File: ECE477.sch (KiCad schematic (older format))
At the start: 54 parts, among them IC1 LP3852EMP-3.3_NOPB, IC5 BQ29330DBT, J1 P7805-2000-S, U1 STM32H7_LQFP144_T2

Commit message: Added Pinout
Added footprints and pinout connections
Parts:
- removed J? (x3): Conn_01x05_Male, symbol Connector:Conn_01x05_Male
- IC5: footprint SOP50P640X120-30N -> SamacSys_Parts:SOP50P640X120-30N
- J2: renamed from J?; footprint (none) -> Connector_PinHeader_1.00mm:PinHeader_1x06_P1.00mm_Vertical
- J3, J4: renamed from J?; footprint (none) -> Connector_PinHeader_1.00mm:PinHeader_1x05_P1.00mm_Vertical
- SW1: renamed from SW?; footprint (none) -> Button_Switch_THT:SW_TH_Tactile_Omron_B3F-10xx
- gave numbers to parts that had none: 3
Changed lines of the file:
@@
 F 0 "IC5" H 9062 1786 50  0000 C CNN
 F 1 "BQ29330DBT" H 9055 1673 50  0000 C CNN
-F 2 "SOP50P640X120-30N" H 19650 4000 50  0001 L CNN
+F 2 "SamacSys_Parts:SOP50P640X120-30N" H 19650 4000 50  0001 L CNN
 F 3 "http://www.ti.com/general/docs/suppproductinfo.tsp?distId=26&gotoUrl=http%3A%2F%2Fwww.ti.com%2Flit%2Fgpn%2Fbq29330" H 19650 3900 50  0001 L CNN
 F 4 "TEXAS INSTRUMENTS - BQ29330DBT. - Li-Ion Battery, Li-Pol Full Protector, 2/3/4 Series, I2C interface, 4.5 V to 28 V supply, TSSOP-30" H 19650 3800 50  0001 L CNN "Description"
@@
 LEDs \nPWR swtch\nmake sure GPIO are ocnnected to advanced timers\n\n\n\n
 $Comp
-L Switch:SW_Push_Dual SW?
+L Switch:SW_Push_Dual SW1
 U 1 1 5F877F07
 P 5850 13350
-F 0 "SW?" H 5850 13635 50  0000 C CNN
+F 0 "SW1" H 5850 13635 50  0000 C CNN
 F 1 "SW_Push_Dual" H 5850 13544 50  0000 C CNN
-F 2 "" H 5850 13550 50  0001 C CNN
+F 2 "Button_Switch_THT:SW_TH_Tactile_Omron_B3F-10xx" H 5850 13550 50  0001 C CNN
 F 3 "~" H 5850 13550 50  0001 C CNN
 	1    5850 13350
@@
 $EndComp
 $Comp
-L pspice:CAP C?
+L pspice:CAP C30
 U 1 1 5F887729
 P 6600 13450
-F 0 "C?" H 6778 13496 50  0000 L CNN
+F 0 "C30" H 6778 13496 50  0000 L CNN
 F 1 ".1uF" H 6778 13405 50  0000 L CNN
 F 2 "Capacitor_SMD:C_0805_2012Metric_Pad1.15x1.40mm_HandSolder" H 6600 13450 50  0001 C CNN
@@
 $EndComp
 $Comp
-L Device:R_US R?
+L Device:R_US R3
 U 1 1 5F8954D3
 P 5850 12600
-F 0 "R?" H 5918 12646 50  0000 L CNN
+F 0 "R3" H 5918 12646 50  0000 L CNN
 F 1 "100k" H 5918 12555 50  0000 L CNN
 F 2 "Resistor_SMD:R_0805_2012Metric_Pad1.15x1.40mm_HandSolder" V 5890 12590 50  0001 C CNN
@@
 VDD_MCU
 $Comp
-L power:GND #PWR?
+L power:GND #PWR05
 U 1 1 5F9369F7
 P 5850 13900
-F 0 "#PWR?" H 5850 13650 50  0001 C CNN
+F 0 "#PWR05" H 5850 13650 50  0001 C CNN
 F 1 "GND" H 5855 13727 50  0000 C CNN
 F 2 "" H 5850 13900 50  0001 C CNN
@@
 NRST
 $Comp
-L Device:R_US R?
+L Device:R_US R4
 U 1 1 5F993DC3
 P 22300 3750
-F 0 "R?" H 22368 3796 50  0000 L CNN
+F 0 "R4" H 22368 3796 50  0000 L CNN
 F 1 "100k" H 22368 3705 50  0000 L CNN
 F 2 "Resistor_SMD:R_0805_2012Metric_Pad1.15x1.40mm_HandSolder" V 22340 3740 50  0001 C CNN
@@
 BOOT0
 $Comp
-L power:GND #PWR?
+L power:GND #PWR06
 U 1 1 5F9EC431
 P 22650 3750
-F 0 "#PWR?" H 22650 3500 50  0001 C CNN
+F 0 "#PWR06" H 22650 3500 50  0001 C CNN
 F 1 "GND" H 22655 3577 50  0000 C CNN
 F 2 "" H 22650 3750 50  0001 C CNN
@@
 $EndComp
 $Comp
-L Connector:Conn_01x06_Male J?
+L Connector:Conn_01x06_Male J2
 U 1 1 5FA28754
 P 10600 8950
-F 0 "J?" H 10708 9331 50  0000 C CNN
+F 0 "J2" H 10708 9331 50  0000 C CNN
 F 1 "Conn_01x05_Male" H 10708 9240 50  0000 C CNN
-F 2 "" H 10600 8950 50  0001 C CNN
+F 2 "Connector_PinHeader_1.00mm:PinHeader_1x06_P1.00mm_Vertical" H 10600 8950 50  0001 C CNN
 F 3 "~" H 10600 8950 50  0001 C CNN
 	1    10600 8950
@@
 $EndComp
 $Comp
-L Connector:Conn_01x05_Male J?
+L Connector:Conn_01x05_Male J4
 U 1 1 5FA2B098
 P 12150 9000
-F 0 "J?" H 12258 9381 50  0000 C CNN
+F 0 "J4" H 12258 9381 50  0000 C CNN
 F 1 "Conn_01x05_Male" H 12258 9290 50  0000 C CNN
-F 2 "" H 12150 9000 50  0001 C CNN
+F 2 "Connector_PinHeader_1.00mm:PinHeader_1x05_P1.00mm_Vertical" H 12150 9000 50  0001 C CNN
 F 3 "~" H 12150 9000 50  0001 C CNN
 	1    12150 9000
@@
 $EndComp
 $Comp
-L Connector:Conn_01x05_Male J?
+L Connector:Conn_01x05_Male J3
 U 1 1 5FA398AC
 P 11800 7550
-F 0 "J?" H 11908 7931 50  0000 C CNN
+F 0 "J3" H 11908 7931 50  0000 C CNN
 F 1 "Conn_01x05_Male" H 11908 7840 50  0000 C CNN
-F 2 "" H 11800 7550 50  0001 C CNN
+F 2 "Connector_PinHeader_1.00mm:PinHeader_1x05_P1.00mm_Vertical" H 11800 7550 50  0001 C CNN
 F 3 "~" H 11800 7550 50  0001 C CNN
 	1    11800 7550
 	1    0    0    -1
 $EndComp
-$Comp
-L Connector:Conn_01x05_Male J?
-U 1 1 5FA48124
-P 15350 10200
-F 0 "J?" H 15458 10581 50  0000 C CNN
-F 1 "Conn_01x05_Male" H 15458 10490 50  0000 C CNN
-F 2 "" H 15350 10200 50  0001 C CNN
-F 3 "~" H 15350 10200 50  0001 C CNN
-	1    15350 10200
-	1    0    0    -1
-$EndComp
-$Comp
-L Connector:Conn_01x05_Male J?
-U 1 1 5FA567D5
-P 16050 10200
-F 0 "J?" H 16158 10581 50  0000 C CNN
-F 1 "Conn_01x05_Male" H 16158 10490 50  0000 C CNN
-F 2 "" H 16050 10200 50  0001 C CNN
-F 3 "~" H 16050 10200 50  0001 C CNN
-	1    16050 10200
-	1    0    0    -1
-$EndComp
-$Comp
-L Connector:Conn_01x05_Male J?
-U 1 1 5FA64E72
-P 16750 10200
-F 0 "J?" H 16858 10581 50  0000 C CNN
-F 1 "Conn_01x05_Male" H 16858 10490 50  0000 C CNN
-F 2 "" H 16750 10200 50  0001 C CNN
-F 3 "~" H 16750 10200 50  0001 C CNN
-	1    16750 10200
-	1    0    0    -1
-$EndComp

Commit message: Updated post review with team members
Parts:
- added J5, J?: Conn_01x05_Male, Connector_PinHeader_1.00mm:PinHeader_1x05_P1.00mm_Vertical, symbol Connector:Conn_01x05_Male
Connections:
- net 5V: now also J5.1 (Pin_1)
- net GND: now also IC5.1 (CELL-), J5.4 (Pin_4)
- net PWM1: now also J?.1 (Pin_1)
- net PWM2: now also J?.2 (Pin_2)
- net PWM3: now also J?.3 (Pin_3)
- net PWM4: now also J?.4 (Pin_4)
- net PWM5: no longer J3.5 (Pin_5)
- net PWR_IN: now also IC5.2 (CELL+), J5.3 (Pin_3)
- net Touch_Input: now also J3.5 (Pin_5), J5.5 (Pin_5), J?.5 (Pin_5)
- net 1V8_VDD renamed OFF
- new net 3.3V: J5.2 (Pin_2)
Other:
- note added: "JTAG - Connection\n"
- note added: "NRST - Switch\n"
- note added: "PWM - Connections\n"
- note added: "USART - Connections\n"
- moved on the sheet: IC5, J2, J3, J4, R4, U1A, U1B

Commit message: Finalized Pinout
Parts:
- removed J?: Conn_01x05_Male, Connector_PinHeader_1.00mm:PinHeader_1x05_P1.00mm_Vertical, symbol Connector:Conn_01x05_Male
- added J6: Conn_01x05_Male, Connector_PinHeader_1.00mm:PinHeader_1x05_P1.00mm_Vertical, symbol Connector:Conn_01x05_Male
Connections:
- net PWM5: now also J3.5 (Pin_5)
- net Touch_Input: no longer J3.5 (Pin_5)
- net V3: now reaches IC5.10 (VC3)
- net V3: now also J6.3 (Pin_3)
- net V2: now reaches IC5.11 (VC2)
- net V2: now also J6.4 (Pin_4)
- net V1: now reaches IC5.12 (VC1)
- net V1: now also J6.5 (Pin_5)
- net V5: now reaches IC5.8 (VC5)
- net V5: now also J6.1 (Pin_1)
- net V4: now reaches IC5.9 (VC4)
- net V4: now also J6.2 (Pin_2)
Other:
- note added: "Bat - Monitor Connections\n"
- note added: "PWR - Input & Output\n"
- note removed: "LEDs \nPWR swtch\nmake sure GPIO are ocnnected to advanced timers\n\n\n\n"
- moved on the sheet: IC5, J2, J4, J5, R1, R2, R4, U1A, U1B, U1C

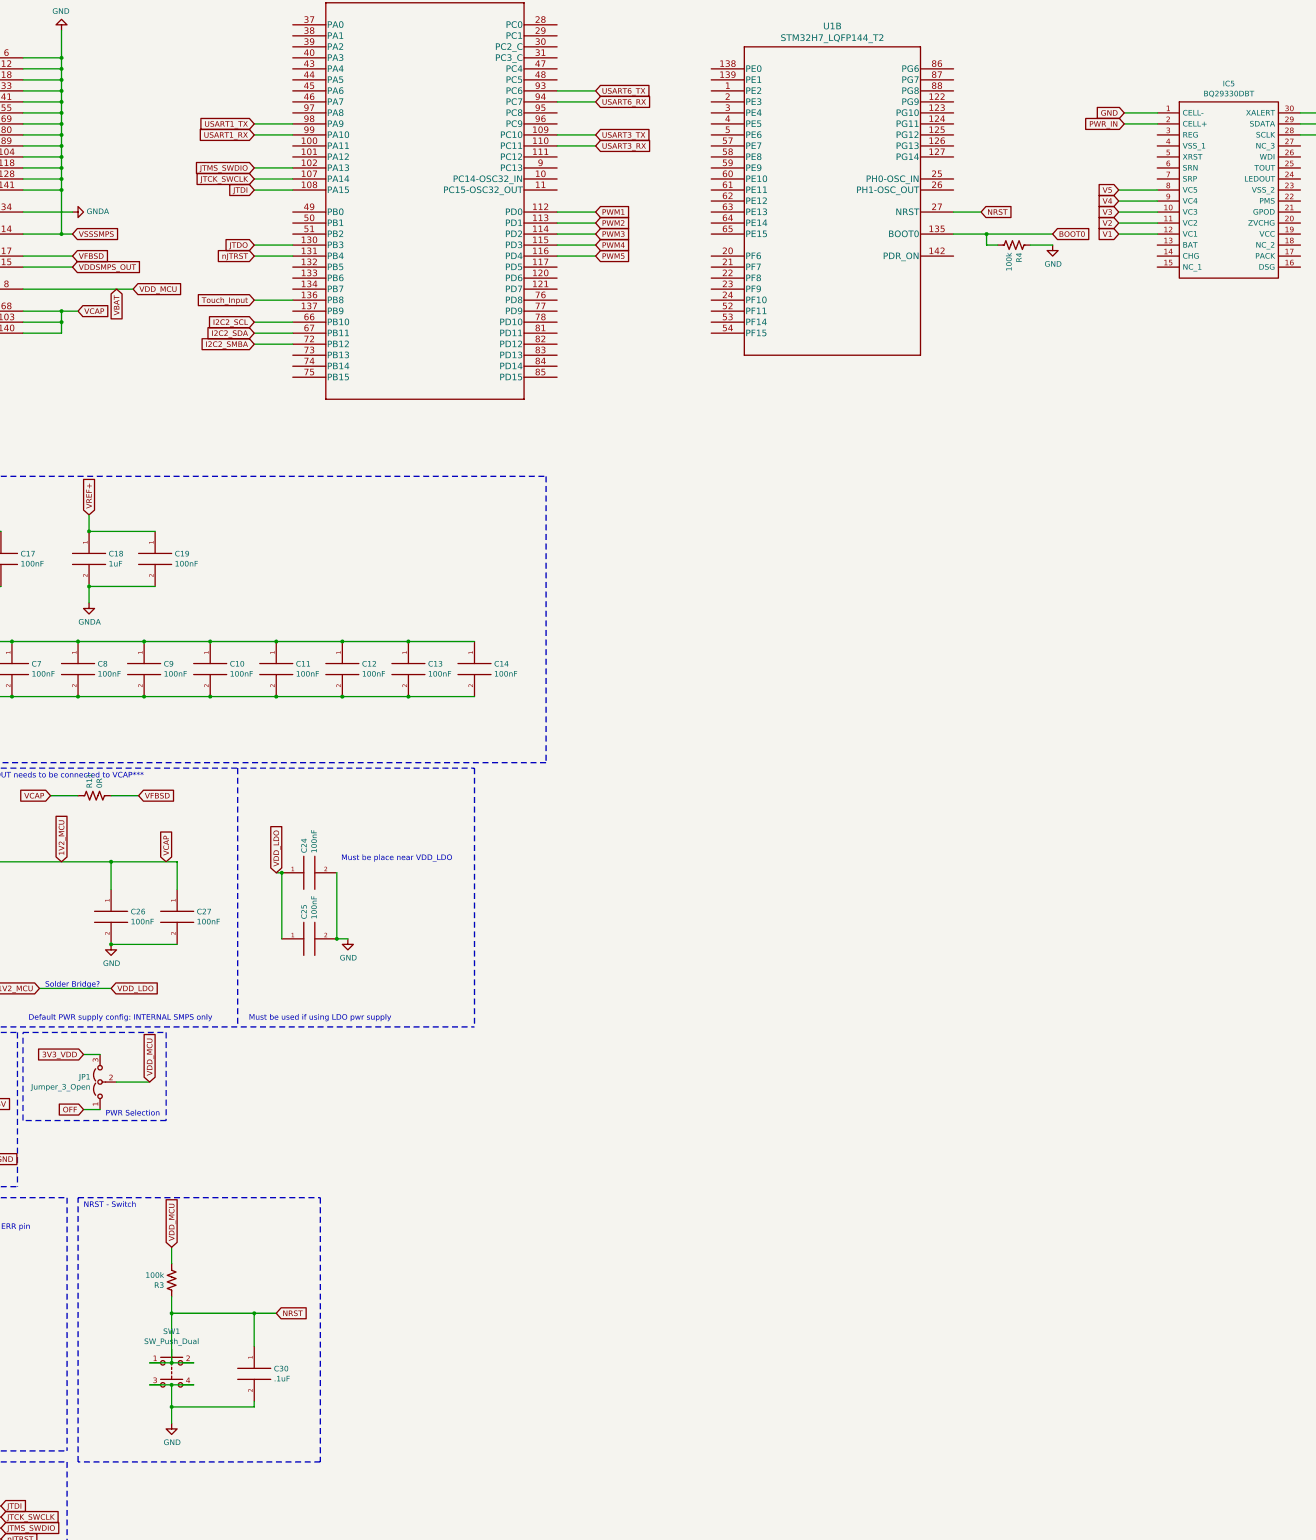
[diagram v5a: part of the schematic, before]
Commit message: Label and layout updates
Updated Labesl for simplicity along with a starting footprint layout for our PCB.
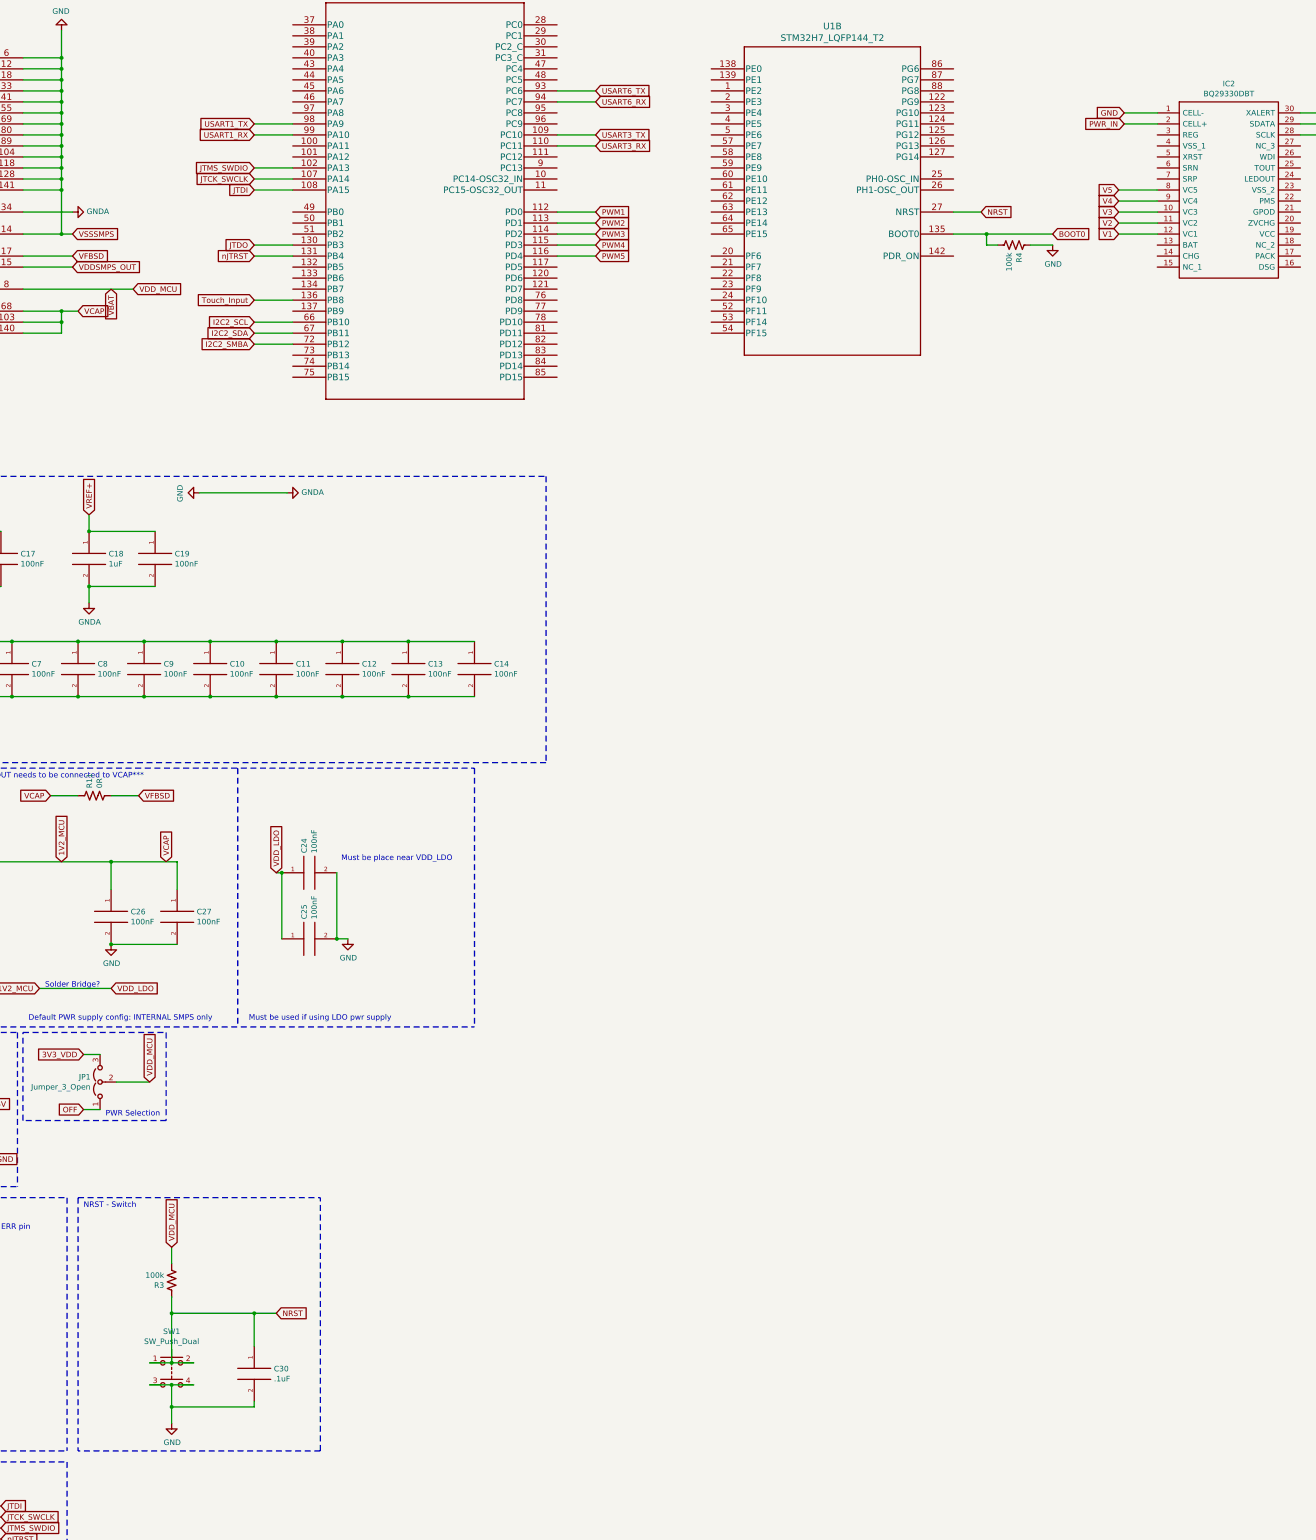
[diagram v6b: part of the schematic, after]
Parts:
- renumbered IC5 to IC2
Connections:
- net GNDA is gone; now on net GND: C16.2, C17.2, C18.2, C19.2, U1.34 (VSSA)

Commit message: Post meeting with TODD
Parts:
- added R5, R6: 0R, Resistor_SMD:R_0805_2012Metric_Pad1.15x1.40mm_HandSolder, symbol Device:R_US
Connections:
- net OFF is gone; now on net GND: JP1.1 (A)
- net 1V2_MCU: now also R6.1; no longer C24.1, C25.1, U1.105 (VDDLDO), U1.143 (VDDLDO), U1.70 (VDDLDO)
- net 3V3_PER: now also R5.2; no longer C29.1, IC1.3 (OUT), JP1.3 (B), R13.2, U1.90 (VDD50USB), U1.91 (VDD33USB)
- new net 3V3_VDD: C29.1, IC1.3 (OUT), JP1.3 (B), R13.2, R5.1, U1.90 (VDD50USB), U1.91 (VDD33USB)
- new net VDD_LDO: C24.1, C25.1, R6.2, U1.105 (VDDLDO), U1.143 (VDDLDO), U1.70 (VDDLDO)
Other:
- note added: "review data sheet for PACK and BAT pions\n"
- note removed: "Solder Bridge?\n"
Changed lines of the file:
@@
 Text GLabel 4650 9950 0    50   Input ~ 0
 1V2_MCU
-Wire Wire Line
-	4650 9950 5300 9950
 Text GLabel 5300 9950 2    50   Input ~ 0
 VDD_LDO
-Text Notes 4700 9950 0    50   ~ 0
-Solder Bridge?\n
 $Comp
 L Jumper:Jumper_3_Open JP1
@@
 Text GLabel 5050 10550 0    50   Input ~ 0
 3V3_VDD
-Text GLabel 5050 11050 0    50   Input ~ 0
-OFF
 Wire Wire Line
 	5350 10800 5650 10800
@@
 Text Notes 600  14100 0    50   ~ 0
 PWR generation blocks for 3.3V power to the MCU  --- NEW LDO \n
-Wire Wire Line
-	2650 13250 3450 13250
-Text GLabel 3450 13250 3    50   Input ~ 0
+Text GLabel 3100 13250 3    50   Input ~ 0
 3V3_VDD
-Text GLabel 3150 13250 3    50   Input ~ 0
+Text GLabel 3600 13250 3    50   Input ~ 0
 3V3_PER
 Text Notes 3000 12150 0    50   ~ 0
@@
 Wire Wire Line
 	2400 13150 2400 13250
-Connection ~ 2650 13250
 Wire Wire Line
 	1900 13250 2400 13250
@@
 Wire Wire Line
 	6100 5450 6900 5450
+$Comp
+L power:GND #PWR0103
+U 1 1 5F983E71
+P 5050 11050
+F 0 "#PWR0103" H 5050 10800 50  0001 C CNN
+F 1 "GND" H 5055 10877 50  0000 C CNN
+F 2 "" H 5050 11050 50  0001 C CNN
+F 3 "" H 5050 11050 50  0001 C CNN
+	1    5050 11050
+	0    1    1    0
+$EndComp
+$Comp
+L Device:R_US R6
+U 1 1 5F9C6E06
+P 4950 9950
+F 0 "R6" H 5018 9996 50  0000 L CNN
+F 1 "0R" H 5018 9905 50  0000 L CNN
+F 2 "Resistor_SMD:R_0805_2012Metric_Pad1.15x1.40mm_HandSolder" V 4990 9940 50  0001 C CNN
+F 3 "~" H 4950 9950 50  0001 C CNN
+	1    4950 9950
+	0    -1   -1   0
+$EndComp
+Wire Wire Line
+	4650 9950 4800 9950
+Wire Wire Line
+	5100 9950 5300 9950
+$Comp
+L Device:R_US R5
+U 1 1 5FA367EF
+P 3350 13250
+F 0 "R5" H 3418 13296 50  0000 L CNN
+F 1 "0R" H 3418 13205 50  0000 L CNN
+F 2 "Resistor_SMD:R_0805_2012Metric_Pad1.15x1.40mm_HandSolder" V 3390 13240 50  0001 C CNN
+F 3 "~" H 3350 13250 50  0001 C CNN
+	1    3350 13250
+	0    -1   -1   0
+$EndComp
+Connection ~ 2650 13250
+Wire Wire Line
+	2650 13250 3200 13250
+Wire Wire Line
+	3500 13250 3600 13250
+Text Notes 14800 4050 0    50   ~ 0
+review data sheet for PACK and BAT pions\n
 $EndSCHEMATC

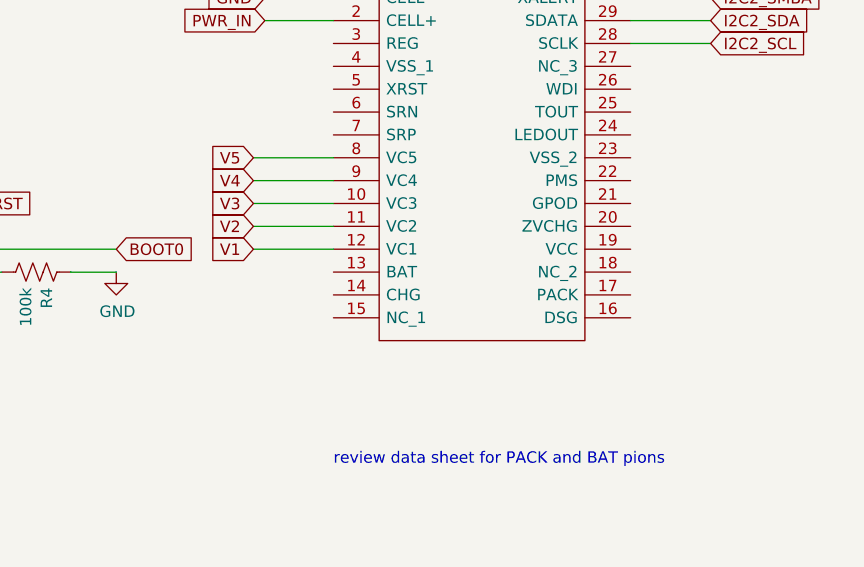
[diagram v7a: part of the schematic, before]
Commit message: Updated PACK and BAT
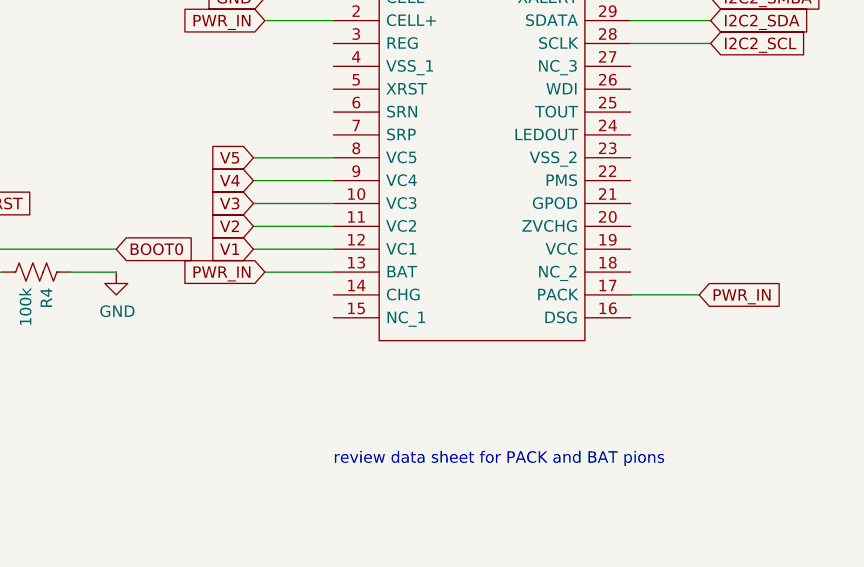
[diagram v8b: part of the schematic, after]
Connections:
- net PWR_IN: now also IC2.13 (BAT), IC2.17 (PACK)
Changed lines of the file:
@@
 Text Notes 14800 4050 0    50   ~ 0
 review data sheet for PACK and BAT pions\n
+Wire Wire Line
+	16100 3300 16400 3300
+Text GLabel 16400 3300 2    50   Input ~ 0
+PWR_IN
+Wire Wire Line
+	14800 3200 14500 3200
+Text GLabel 14500 3200 0    50   Input ~ 0
+PWR_IN
 $EndSCHEMATC
